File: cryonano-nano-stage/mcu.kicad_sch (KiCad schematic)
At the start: 2 parts, among them U1 2DIB0410FXUMA1, U2 2DIB1410FXUMA1

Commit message: preliminary components added
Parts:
- removed U1: 2DIB0410FXUMA1, SOIC127P600X175-8N, symbol symbols:2DIB0410FXUMA1
- removed U2: 2DIB1410FXUMA1, SOIC127P600X175-8N, symbol symbols:2DIB1410FXUMA1
- added C11: 10uF, Capacitor_SMD:C_0805_2012Metric, symbol Device:C_Small
- added C14, C15, C5, C64, C7: 0.1uF, Capacitor_SMD:C_0603_1608Metric, symbol Device:C_Small
- added C20, C36: 22pF, Capacitor_SMD:C_0603_1608Metric, symbol Device:C_Small
- added FB3: MH1608, Inductor_SMD:L_0603_1608Metric, symbol Device:FerriteBead
- added J8: Conn_ST_STDC14, footprints:PinHeader_2x07_P1.27mm_Vertical, symbol symbols:Conn_ST_STDC14
- added LED3: RGB-CA, footprints:19037ARSGHBHW1S032T, symbol symbols:19-037A_RSGHBHW1-S03_2T
- added R11, R35, R8: 47k, Resistor_SMD:R_0603_1608Metric, symbol Device:R_Small
- added R29, R30, R31, R32, R33, R34: 22R, Resistor_SMD:R_0603_1608Metric, symbol Device:R_Small
- added R5: 10k, Resistor_SMD:R_0603_1608Metric, symbol Device:R_Small
- added R9: 1k, Resistor_SMD:R_0603_1608Metric, symbol Device:R_Small
- added SW1: ~{RESET}, Button_Switch_SMD:SW_Tactile_SPST_NO_Straight_CK_PTS636Sx25SMTRLFS, symbol Switch:SW_Push
- added SW2: BOOT0, Button_Switch_SMD:SW_Tactile_SPST_NO_Straight_CK_PTS636Sx25SMTRLFS, symbol Switch:SW_Push
- added U5: STM32L412CBT6P, Package_QFP:LQFP-32_7x7mm_P0.8mm, symbol symbols:STM32L412CBT6P
- added U9: LP5817DRLR, footprints:LP5817DRLR, symbol symbols:LP5817DRLR
- added Y1: Crystal, Crystal:Crystal_SMD_3215-2Pin_3.2x1.5mm, symbol Device:Crystal
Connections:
- new net: R9.2, SW2.2
- new net: C36.1, Y1.1
- new net: C20.1, Y1.2
- new net +3V3IN: FB3.1
- new net +3V3V: C11.1, C14.1, C15.1, FB3.2, J8.3 (VCC), R11.2, R35.2, R5.1, R9.1
- new net +5V0IN: C64.1, LED3.4 (ANODE), U9.4 (VCC)
- new net BOOT0: C7.1, R8.2, SW2.1
- new net CLKADC: R33.1
- new net GND: C11.2, C14.2, C15.2, C20.2, C36.2, C5.2, C64.2, C7.2, J8.11 (GNDDetect), J8.5 (GND), J8.7 (GND), R8.1, SW1.2, U9.3 (GND)
- new net SCK: R30.1
- new net SDI: R32.1
- new net SDO: R31.1
- new net STATUS_B: LED3.3 (B), U9.8 (OUT0)
- new net STATUS_G: LED3.2 (G), U9.7 (OUT1)
- new net STATUS_R: LED3.1 (R), U9.6 (OUT2)
- new net STATUS_RGB_SCL: R11.1, U9.1 (SCL)
- new net STATUS_RGB_SDA: R35.1, U9.2 (SDA)
- new net T_JCLK/T_SWCLK: J8.6 (JCLK/SWCLK)
- new net T_JTDO/T_SWO: J8.8 (JTDO/SWO)
- new net T_JTMS/T_SWDIO : J8.4 (JTMS/SWDIO)
- new net T_NRST: C5.1, J8.12 (~{RST}), R5.2, SW1.1
- new net T_VCP_RX: J8.13 (VCP_RX(TX))
- new net T_VCP_TX: J8.14 (VCP_TX(RX))
- new net ~{CS}: R29.1
- new net ~{IRQ}: R34.1
- no-connect marks 0 -> 9
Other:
- note added: "SWD WITH TRACE"

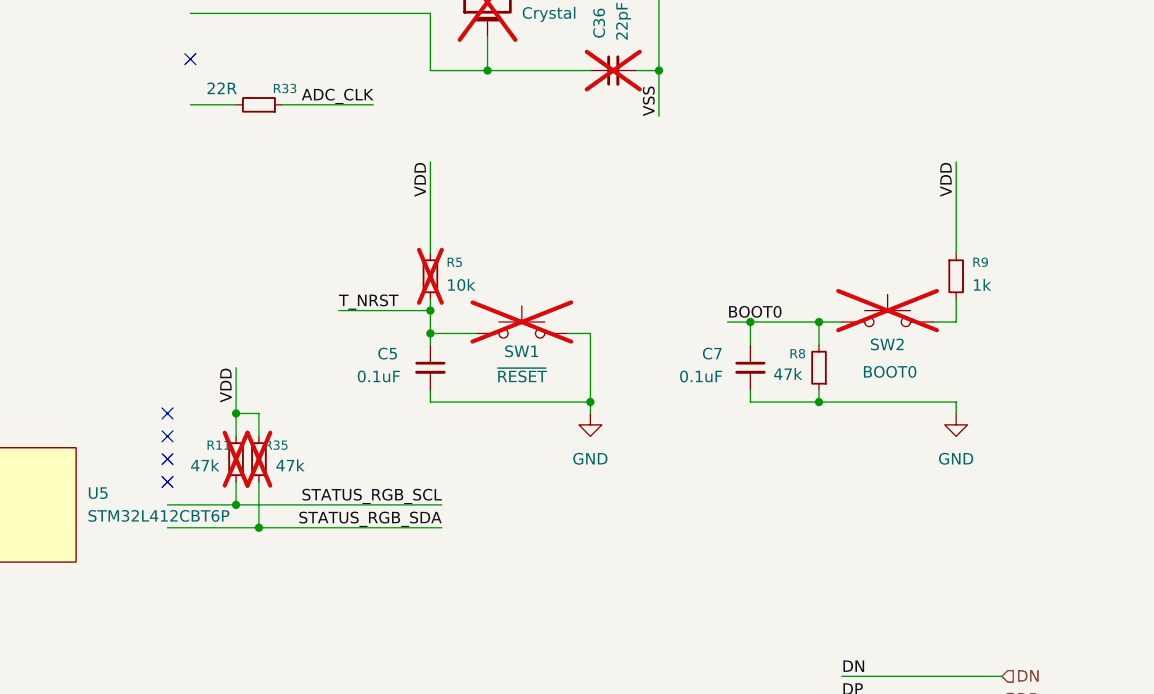
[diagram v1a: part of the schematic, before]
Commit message: schematic cleaned
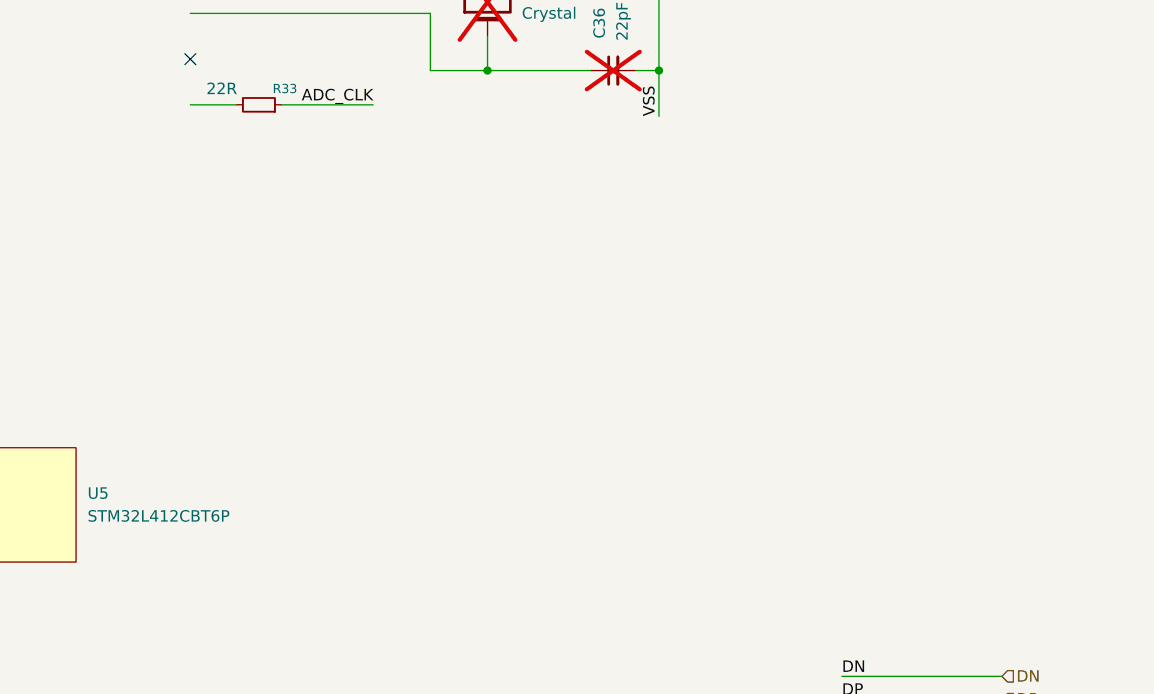
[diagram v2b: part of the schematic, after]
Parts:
- removed C5, C7: 0.1uF, Capacitor_SMD:C_0603_1608Metric, symbol Device:C_Small
- removed R11, R35, R8: 47k, Resistor_SMD:R_0603_1608Metric, symbol Device:R_Small
- removed R5: 10k, Resistor_SMD:R_0603_1608Metric, symbol Device:R_Small
- removed R9: 1k, Resistor_SMD:R_0603_1608Metric, symbol Device:R_Small
- removed SW1: ~{RESET}, Button_Switch_SMD:SW_Tactile_SPST_NO_Straight_CK_PTS636Sx25SMTRLFS, symbol Switch:SW_Push
- removed SW2: BOOT0, Button_Switch_SMD:SW_Tactile_SPST_NO_Straight_CK_PTS636Sx25SMTRLFS, symbol Switch:SW_Push
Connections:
- no-connect marks 9 -> 5

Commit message: sch updated
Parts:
- removed LED3: RGB-CA, footprints:19037ARSGHBHW1S032T, symbol symbols:19-037A_RSGHBHW1-S03_2T
- removed R29, R30, R31, R32, R33, R34: 22R, Resistor_SMD:R_0603_1608Metric, symbol Device:R_Small
- removed U5: STM32L412CBT6P, Package_QFP:LQFP-32_7x7mm_P0.8mm, symbol symbols:STM32L412CBT6P
- removed U9: LP5817DRLR, footprints:LP5817DRLR, symbol symbols:LP5817DRLR
- added C16, C17: 0.1uF, Capacitor_SMD:C_0603_1608Metric, symbol Device:C_Small
- added C21, C37: 22pF, Capacitor_SMD:C_0603_1608Metric, symbol Device:C_Small
- added R35: 470R, Resistor_SMD:R_0603_1608Metric, symbol Device:R_Small
- added R36, R38: 10k, Resistor_SMD:R_0603_1608Metric, symbol Device:R_Small
- added SW1: BOOT, symbol Switch:SW_Push
- added SW2: RESET, symbol Switch:SW_Push
- added U2: STM32L412CxTx, QFP50P900X900X160-48N, symbol symbols:STM32L412CxTx
- added Y2: Crystal, Crystal:Crystal_SMD_3215-2Pin_3.2x1.5mm, symbol Device:Crystal
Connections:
- net +3V3V: now also R35.1, R38.1, U2.24 (VDD_1), U2.48 (VDD_2)
- net BOOT0: now also C16.1, R36.1, SW1.2, U2.44 (PH3/BOOT0)
- net DP: now also U2.33 (PA12/DP)
- net GND: now also C16.2, C17.2, C21.2, C37.2, R36.2, SW2.2; no longer C20.2, C36.2
- net at C36.1, Y1.1: now also U2.4 (PC15/OSC32_OUT)
- net at C20.1, Y1.2: now also U2.3 (PC14/OSC32_IN)
- net T_JCLK/T_SWCLK renamed SWCLK
- net SWCLK: now also U2.37 (PA14/SWCLK)
- net T_JTDO/T_SWO renamed SWO
- net SWO: now also U2.39 (PB3/SWO)
- net T_JTMS/T_SWDIO  renamed SWDIO
- net SWDIO: now also U2.34 (PA13/SWDIO)
- net T_NRST renamed NRST
- net NRST: now also C17.1, R38.2, SW2.1, U2.7 (NRST)
- net T_VCP_RX renamed LOG_RX
- net LOG_RX: now also U2.12 (PA2/USART2_TX)
- net T_VCP_TX renamed LOG_TX
- net LOG_TX: now also U2.13 (PA3/USART2_RX)
- new net: C20.2, C36.2
- new net: C37.1, U2.6 (PH1/OSC_OUT), Y2.1
- new net: C21.1, U2.5 (PH0/OSC_IN), Y2.2
- new net: R35.2, SW1.1
- new net DM: U2.32 (PA11/DM)
- new net VBAT: U2.1 (VBAT)
- new net VDDA: U2.9 (VDDA)
- new net VDDUSB: U2.36 (VDDUSB)
- new net VSSA: U2.8 (VSSA)
- new net VSS_1: U2.23 (VSS_1)
- new net VSS_2: U2.35 (VSS_2)
- new net VSS_3: U2.47 (VSS_3)
- no-connect marks 5 -> 3
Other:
- note added: "BOOT memory selection."
- note added: "MCU"
- note added: "MCU reset."
- note added: "Power conditioning."
- note added: "SIGNALS"
- moved on the sheet: C20, C36, C64, J8, Y1

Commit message: schematic cleaned
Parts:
- C20, C21, C36, C37: Unit Price for 10pcs 0.973 -> (none)
